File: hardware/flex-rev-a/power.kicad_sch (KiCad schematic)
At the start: 0 parts

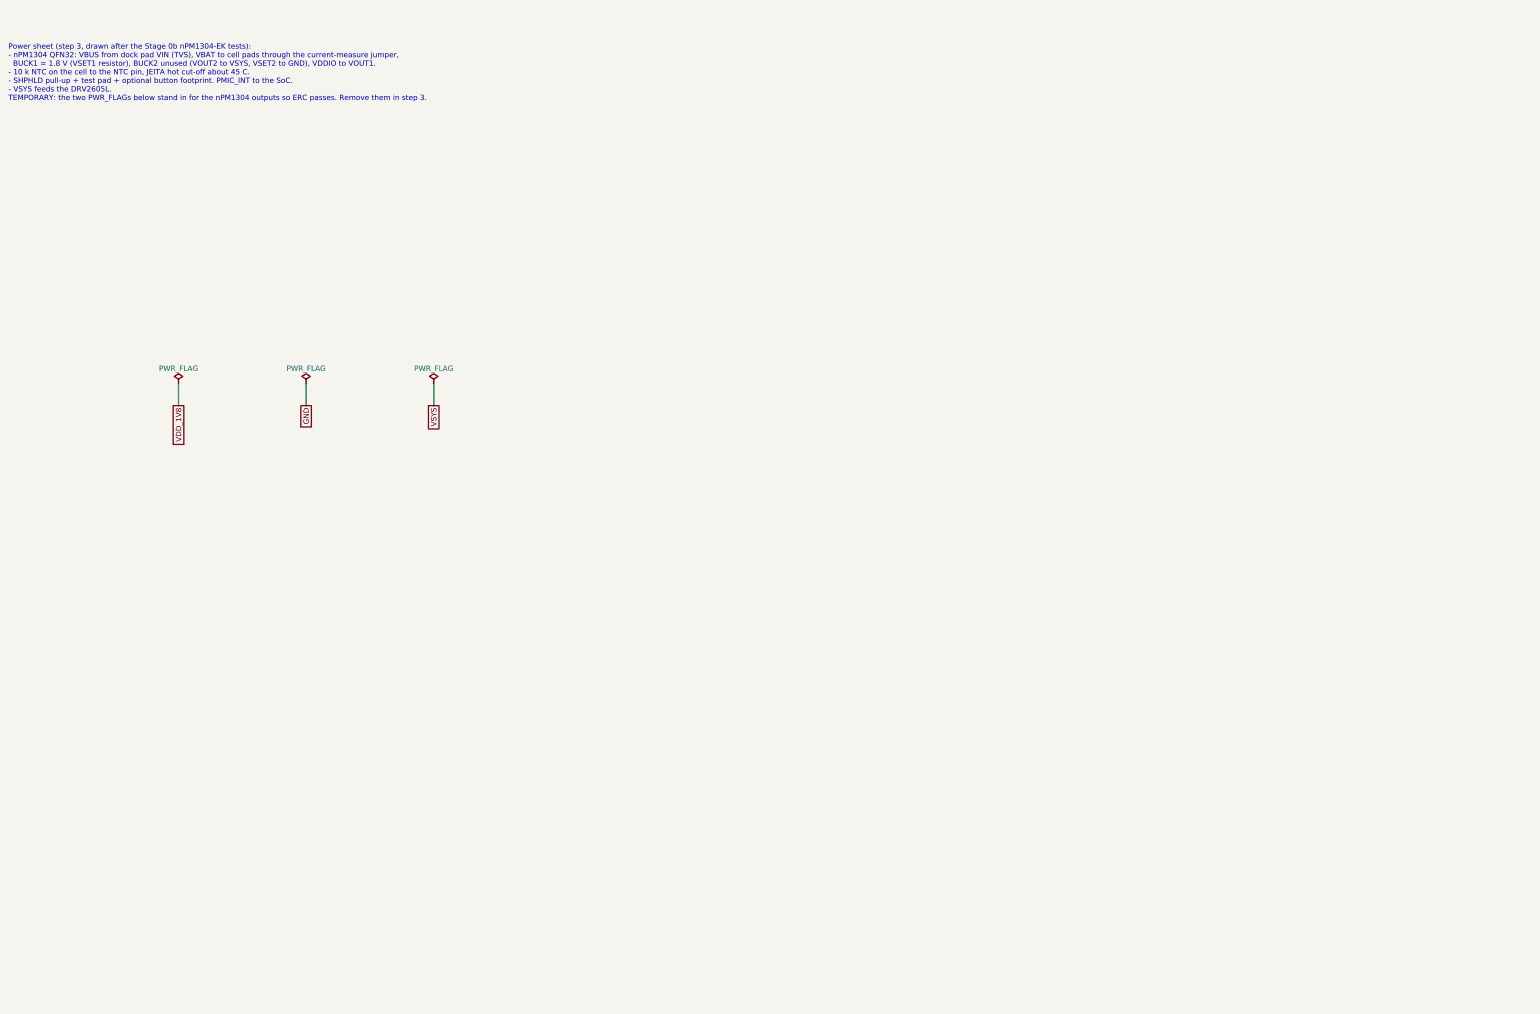
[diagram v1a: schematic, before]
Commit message: Draw nPM1304 power sheet and move the project to KiCad 10 format
Power sheet (step 3 of the flex plan), from Nordic's nPM1304 datasheet
reference circuit "configuration 2" (QFN32):
- VBUS from dock VIN with a TVS and 1 uF; CC1/CC2 to GND (no USB-C).
- VBAT to the cell pads through a cut-able current-measure jumper (JP201).
- BUCK1 at 1.8 V (VSET1 47k, confirmed in the datasheet table) on VDD_1V8,
  2.2 uH + 10 uF; VDDIO from VOUT1; PVSS1 to GND through a net tie.
- BUCK2 unused: VOUT2 to VSYS, VSET2 and PVSS2 to GND, SW2 open, no inductor.
  Load switches unused (pins to GND), LED pins open.
- 10k B3380 NTC, SHPHLD test pad + DNP pull-up and button footprint,
  PMIC_INT on GPIO3, 4.7k I2C pull-ups for the shared 1.8 V bus.
- Temporary PWR_FLAGs on VDD_1V8 and VSYS removed (now driven by the PMIC);
  flags remain only on off-board sources (VIN, cell VBAT/GND) and PVSS1.
- Open items marked (check) on the sheet.

Also: nPM1304-QEAA symbol added to wakeband.kicad_sym, all sheets and the
library saved in KiCad 10 format, PDF replotted, README ERC status, plan
notes updated with datasheet facts (TWI 0x6B, VBUS exits ship mode).

ERC (KiCad 10.0.5): 2 errors, 10 warnings, none on the power sheet; all
wait for the dock/sensors/haptics/debug sheets.

Co-Authored-By: Claude Opus 5.5 <noreply@anthropic.com>
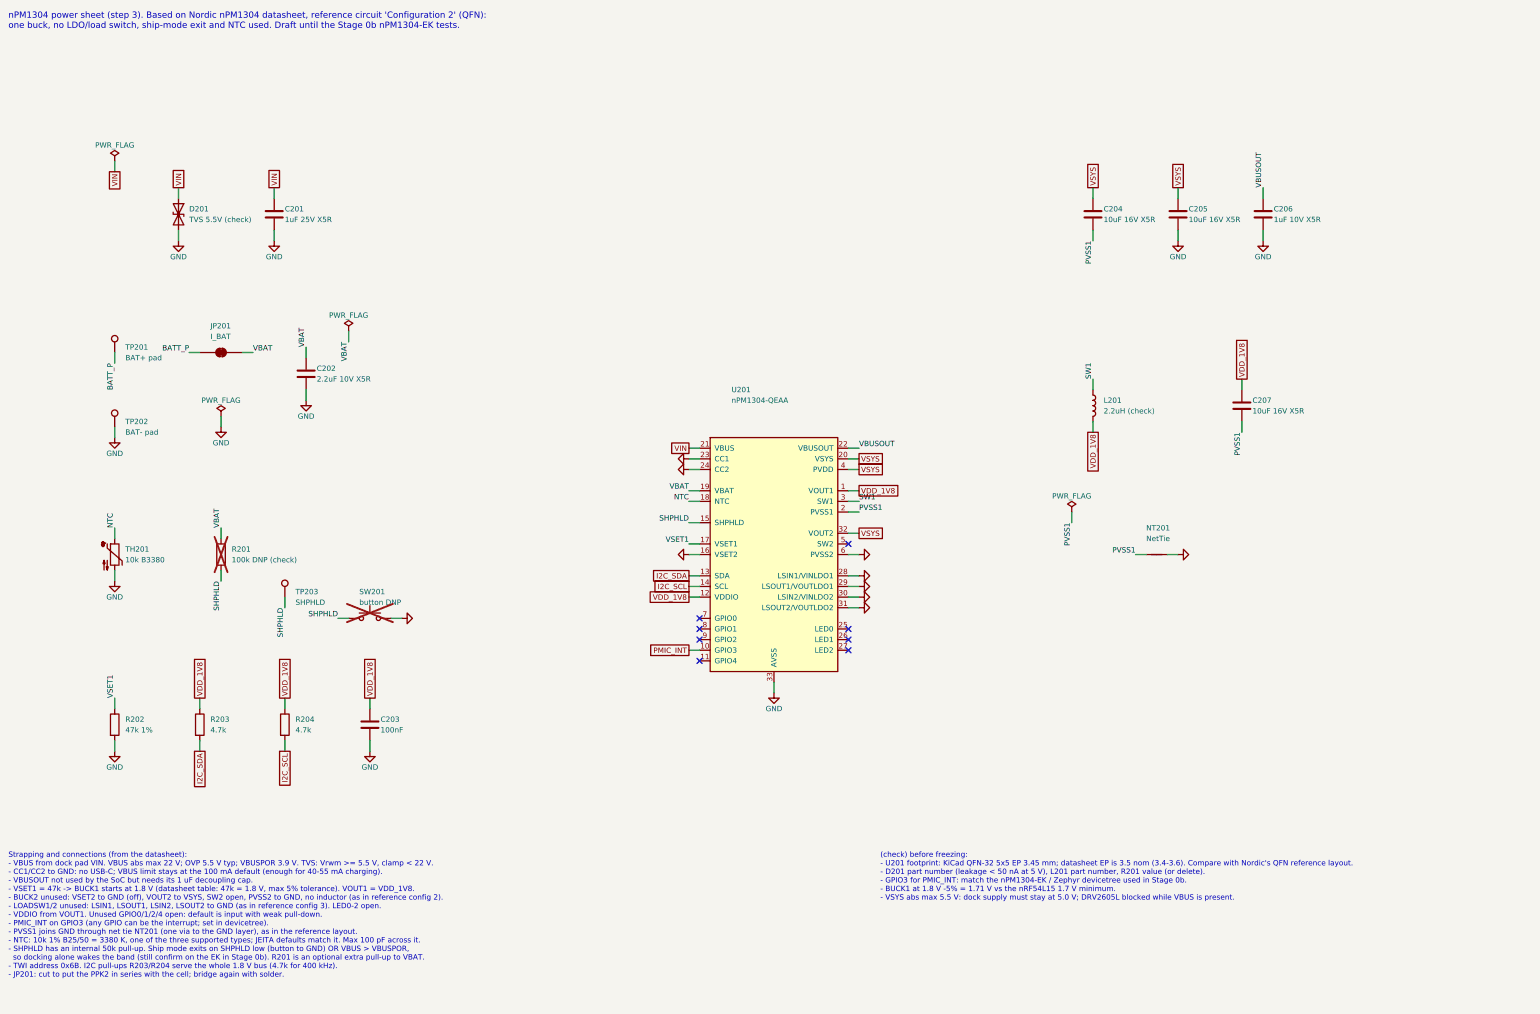
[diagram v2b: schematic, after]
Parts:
- added C201: 1uF 25V X5R, Capacitor_SMD:C_0603_1608Metric, symbol Device:C
- added C202: 2.2uF 10V X5R, Capacitor_SMD:C_0603_1608Metric, symbol Device:C
- added C203: 100nF, Capacitor_SMD:C_0402_1005Metric, symbol Device:C
- added C204, C205, C207: 10uF 16V X5R, Capacitor_SMD:C_0603_1608Metric, symbol Device:C
- added C206: 1uF 10V X5R, Capacitor_SMD:C_0603_1608Metric, symbol Device:C
- added D201: TVS 5.5V (check), Diode_SMD:D_0402_1005Metric, symbol Device:D_TVS
- added JP201: I_BAT, Jumper:SolderJumper-2_P1.3mm_Bridged_RoundedPad1.0x1.5mm, symbol Jumper:SolderJumper_2_Bridged
- added L201: 2.2uH (check), Inductor_SMD:L_Murata_DFE201610P, symbol Device:L
- added NT201: NetTie, NetTie:NetTie-2_SMD_Pad0.5mm, symbol Device:NetTie_2
- added R201: 100k DNP (check), Resistor_SMD:R_0402_1005Metric, symbol Device:R
- added R202: 47k 1%, Resistor_SMD:R_0402_1005Metric, symbol Device:R
- added R203, R204: 4.7k, Resistor_SMD:R_0402_1005Metric, symbol Device:R
- added SW201: button DNP, Button_Switch_SMD:SW_SPST_B3U-1000P, symbol Switch:SW_Push
- added TH201: 10k B3380, Resistor_SMD:R_0402_1005Metric, symbol Device:Thermistor_NTC
- added TP201: BAT+ pad, TestPoint:TestPoint_Pad_2.0x2.0mm, symbol Connector:TestPoint
- added TP202: BAT- pad, TestPoint:TestPoint_Pad_2.0x2.0mm, symbol Connector:TestPoint
- added TP203: SHPHLD, TestPoint:TestPoint_Pad_1.0x1.0mm, symbol Connector:TestPoint
- added U201: nPM1304-QEAA, Package_DFN_QFN:QFN-32-1EP_5x5mm_P0.5mm_EP3.45x3.45mm, symbol wakeband:nPM1304-QEAA
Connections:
- net GND: now also C201.2, C202.2, C203.2, C205.2, C206.2, D201.2 (A2), NT201.2, R202.2, SW201.2, TH201.2, TP202.1, U201.16 (VSET2), U201.23 (CC1), U201.24 (CC2), U201.28 (LSIN1/VINLDO1), U201.29 (LSOUT1/VOUTLDO1), U201.30 (LSIN2/VINLDO2), U201.31 (LSOUT2/VOUTLDO2), U201.33 (AVSS), U201.6 (PVSS2)
- net VDD_1V8: now also C203.1, C207.1, L201.2, R203.1, R204.1, U201.1 (VOUT1), U201.12 (VDDIO)
- net VSYS: now also C204.1, C205.1, U201.20 (VSYS), U201.32 (VOUT2), U201.4 (PVDD)
- new net BATT_P: JP201.1 (A), TP201.1
- new net I2C_SCL: R204.2, U201.14 (SCL)
- new net I2C_SDA: R203.2, U201.13 (SDA)
- new net NTC: TH201.1, U201.18 (NTC)
- new net PMIC_INT: U201.10 (GPIO3)
- new net PVSS1: C204.2, C207.2, NT201.1, U201.2 (PVSS1)
- new net SHPHLD: R201.2, SW201.1, TP203.1, U201.15 (SHPHLD)
- new net SW1: L201.1, U201.3 (SW1)
- new net VBAT: C202.1, JP201.2 (B), R201.1, U201.19 (VBAT)
- new net VBUSOUT: C206.1, U201.22 (VBUSOUT)
- new net VIN: C201.1, D201.1 (A1), U201.21 (VBUS)
- new net VSET1: R202.1, U201.17 (VSET1)
- no-connect marks 0 -> 8
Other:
- note added: "(check) before freezing: - U201 footprint: KiCad QFN-32 5x5 EP 3.45 mm; datasheet EP is 3.5 nom (3.4-3.6). Compare with Nordic's QFN reference layout. - D201 part number (leakage < 50 nA at 5 V), L201 part number, R201 value (or delete). - GPIO3 for PMIC_INT: match the nPM1304-EK / Zephyr devicetree used in Stage 0b. - BUCK1 at 1.8 V -5% = 1.71 V vs the nRF54L15 1.7 V minimum. - VSYS abs max 5.5 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"
- note added: "Strapping and connections (from the datasheet): - VBUS from dock pad VIN. VBUS abs max 22 V; OVP 5.5 V typ; VBUSPOR 3.9 V. TVS: Vrwm >= 5.5 V, clamp < 22 V. - CC1/CC2 to GND: no USB-C; VBUS limit stays at the 100 mA default (enough for 40-55 mA charging). - VBUSOUT not used by the SoC but needs its 1 uF decoupling cap. - VSET1 = 47k -> BUCK1 starts at 1.8 V (datasheet table: 47k = 1.8 V, max 5% t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"
- note added: "nPM1304 power sheet (step 3). Based on Nordic nPM1304 datasheet, reference circuit 'Configuration 2' (QFN): one buck, no LDO/load switch, ship-mode exit and NTC used. Draft until the Stage 0b nPM1304-EK tests."
- note removed: "Power sheet (step 3, drawn after the Stage 0b nPM1304-EK tests): - nPM1304 QFN32: VBUS from dock pad VIN (TVS), VBAT to cell pads through the current-measure jumper, BUCK1 = 1.8 V (VSET1 resistor), BUCK2 unused (VOUT2 to VSYS, VSET2 to GND), VDDIO to VOUT1. - 10 k NTC on the cell to the NTC pin, JEITA hot cut-off about 45 C. - SHPHLD pull-up + test pad + optional button footprint. PMIC_INT to the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"

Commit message: Power sheet: record SHPHLD decision, add LCSC numbers, make VBAT global
- SHPHLD relies on the nPM1304's internal 50k pull-up; R201 and SW201 stay
  DNP (noted on the sheet).
- LCSC part numbers on the passives, NTC, inductor, TVS and button; pads,
  jumper and net tie excluded from the BOM.
- VBAT is now a global label so the debug sheet can give it a test pad.
- 10 uF caps changed to a 25 V part (CL10A106MA8NRNC) that LCSC stocks.

Co-Authored-By: Claude Opus 5.5 <noreply@anthropic.com>
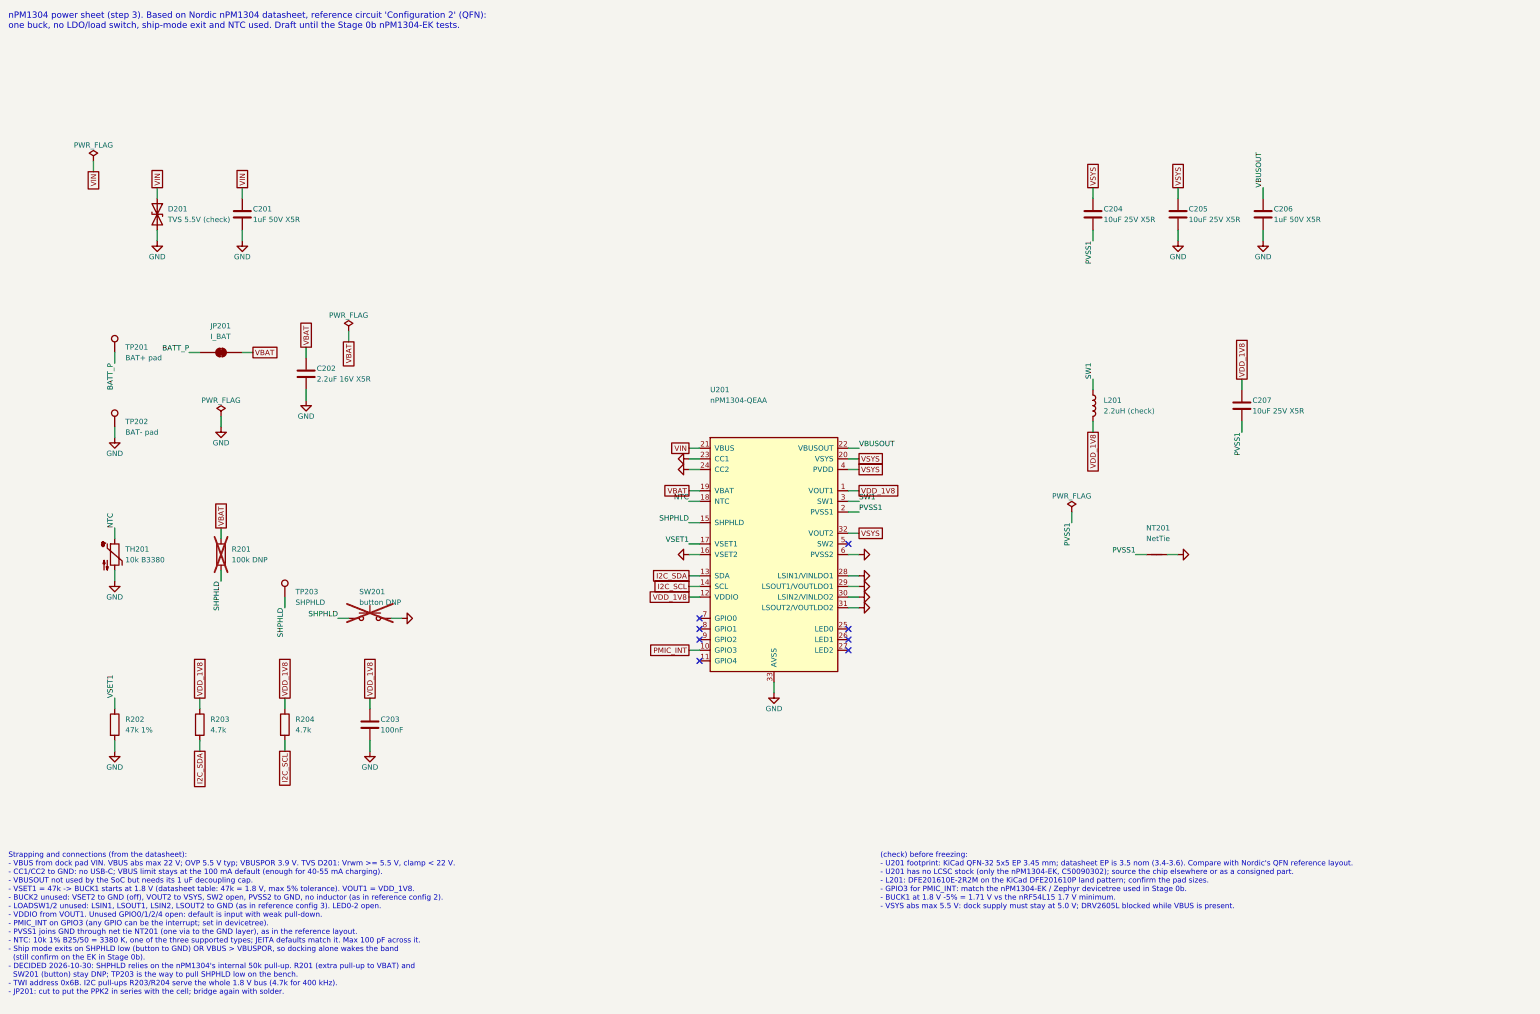
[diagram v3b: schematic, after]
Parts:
- C201: value 1uF 25V X5R -> 1uF 50V X5R; LCSC (none) -> C15849
- C202: value 2.2uF 10V X5R -> 2.2uF 16V X5R; LCSC (none) -> C23630
- C203: LCSC (none) -> C1525
- C204, C205, C207: value 10uF 16V X5R -> 10uF 25V X5R; LCSC (none) -> C96446
- C206: value 1uF 10V X5R -> 1uF 50V X5R; LCSC (none) -> C15849
- D201: LCSC (none) -> C48260
- JP201, NT201, TP201, TP202, TP203: now left out of the parts list
- L201: LCSC (none) -> C337891; MPN (none) -> Murata DFE201610E-2R2M
- R201: value 100k DNP (check) -> 100k DNP; LCSC (none) -> C25741
- R202: LCSC (none) -> C25792
- R203, R204: LCSC (none) -> C25900
- SW201: LCSC (none) -> C231329; MPN (none) -> Omron B3U-1000P
- TH201: LCSC (none) -> C77131; MPN (none) -> Murata NCP15XH103F03RC
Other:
- note added: "(check) before freezing: - U201 footprint: KiCad QFN-32 5x5 EP 3.45 mm; datasheet EP is 3.5 nom (3.4-3.6). Compare with Nordic's QFN reference layout. - U201 has no LCSC stock (only the nPM1304-EK, C50090302); source the chip elsewhere or as a consigned part. - L201: DFE201610E-2R2M on the KiCad DFE201610P land pattern; confirm the pad sizes. - GPIO3 for PMIC_INT: match the nPM1304-EK / Zephyr de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"
- note added: "Strapping and connections (from the datasheet): - VBUS from dock pad VIN. VBUS abs max 22 V; OVP 5.5 V typ; VBUSPOR 3.9 V. TVS D201: Vrwm >= 5.5 V, clamp < 22 V. - CC1/CC2 to GND: no USB-C; VBUS limit stays at the 100 mA default (enough for 40-55 mA charging). - VBUSOUT not used by the SoC but needs its 1 uF decoupling cap. - VSET1 = 47k -> BUCK1 starts at 1.8 V (datasheet table: 47k = 1.8 V, max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"
- note removed: "(check) before freezing: - U201 footprint: KiCad QFN-32 5x5 EP 3.45 mm; datasheet EP is 3.5 nom (3.4-3.6). Compare with Nordic's QFN reference layout. - D201 part number (leakage < 50 nA at 5 V), L201 part number, R201 value (or delete). - GPIO3 for PMIC_INT: match the nPM1304-EK / Zephyr devicetree used in Stage 0b. - BUCK1 at 1.8 V -5% = 1.71 V vs the nRF54L15 1.7 V minimum. - VSYS abs max 5.5 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"
- note removed: "Strapping and connections (from the datasheet): - VBUS from dock pad VIN. VBUS abs max 22 V; OVP 5.5 V typ; VBUSPOR 3.9 V. TVS: Vrwm >= 5.5 V, clamp < 22 V. - CC1/CC2 to GND: no USB-C; VBUS limit stays at the 100 mA default (enough for 40-55 mA charging). - VBUSOUT not used by the SoC but needs its 1 uF decoupling cap. - VSET1 = 47k -> BUCK1 starts at 1.8 V (datasheet table: 47k = 1.8 V, max 5% t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"
